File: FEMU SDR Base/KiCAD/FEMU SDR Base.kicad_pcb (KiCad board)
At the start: 4 copper layers, 164.8 x 186.6 mm, 69 parts, among them P10 PWM2, P11 PWM3, P12 PWM4, P13 PWM1, P14 PWM2, P15 PWM3, P16 PWM4, P17 12V, P18 GND, P19 12V, P2 SDR_Shield_1, P20 GND, P21 S0GND, P22 S1GND, P23 S0DN, P24 S1DN, P25 S0DP, P26 S1DP, P27 PWM0, P28 PWM5, P29 PWM6, P3 SDR_Shield_2, P30 PWM7, P31 PWM0, P32 PWM5, P33 PWM6, P34 PWM7, P4 12V, P5 GND, P6 12V, P7 GND, P8 Raspi_Power_Shield, P9 PWM1, U1 TPS562209, U2 LP38858-LDO, U3 LP38858-LDO, U4 7833, U5 7833

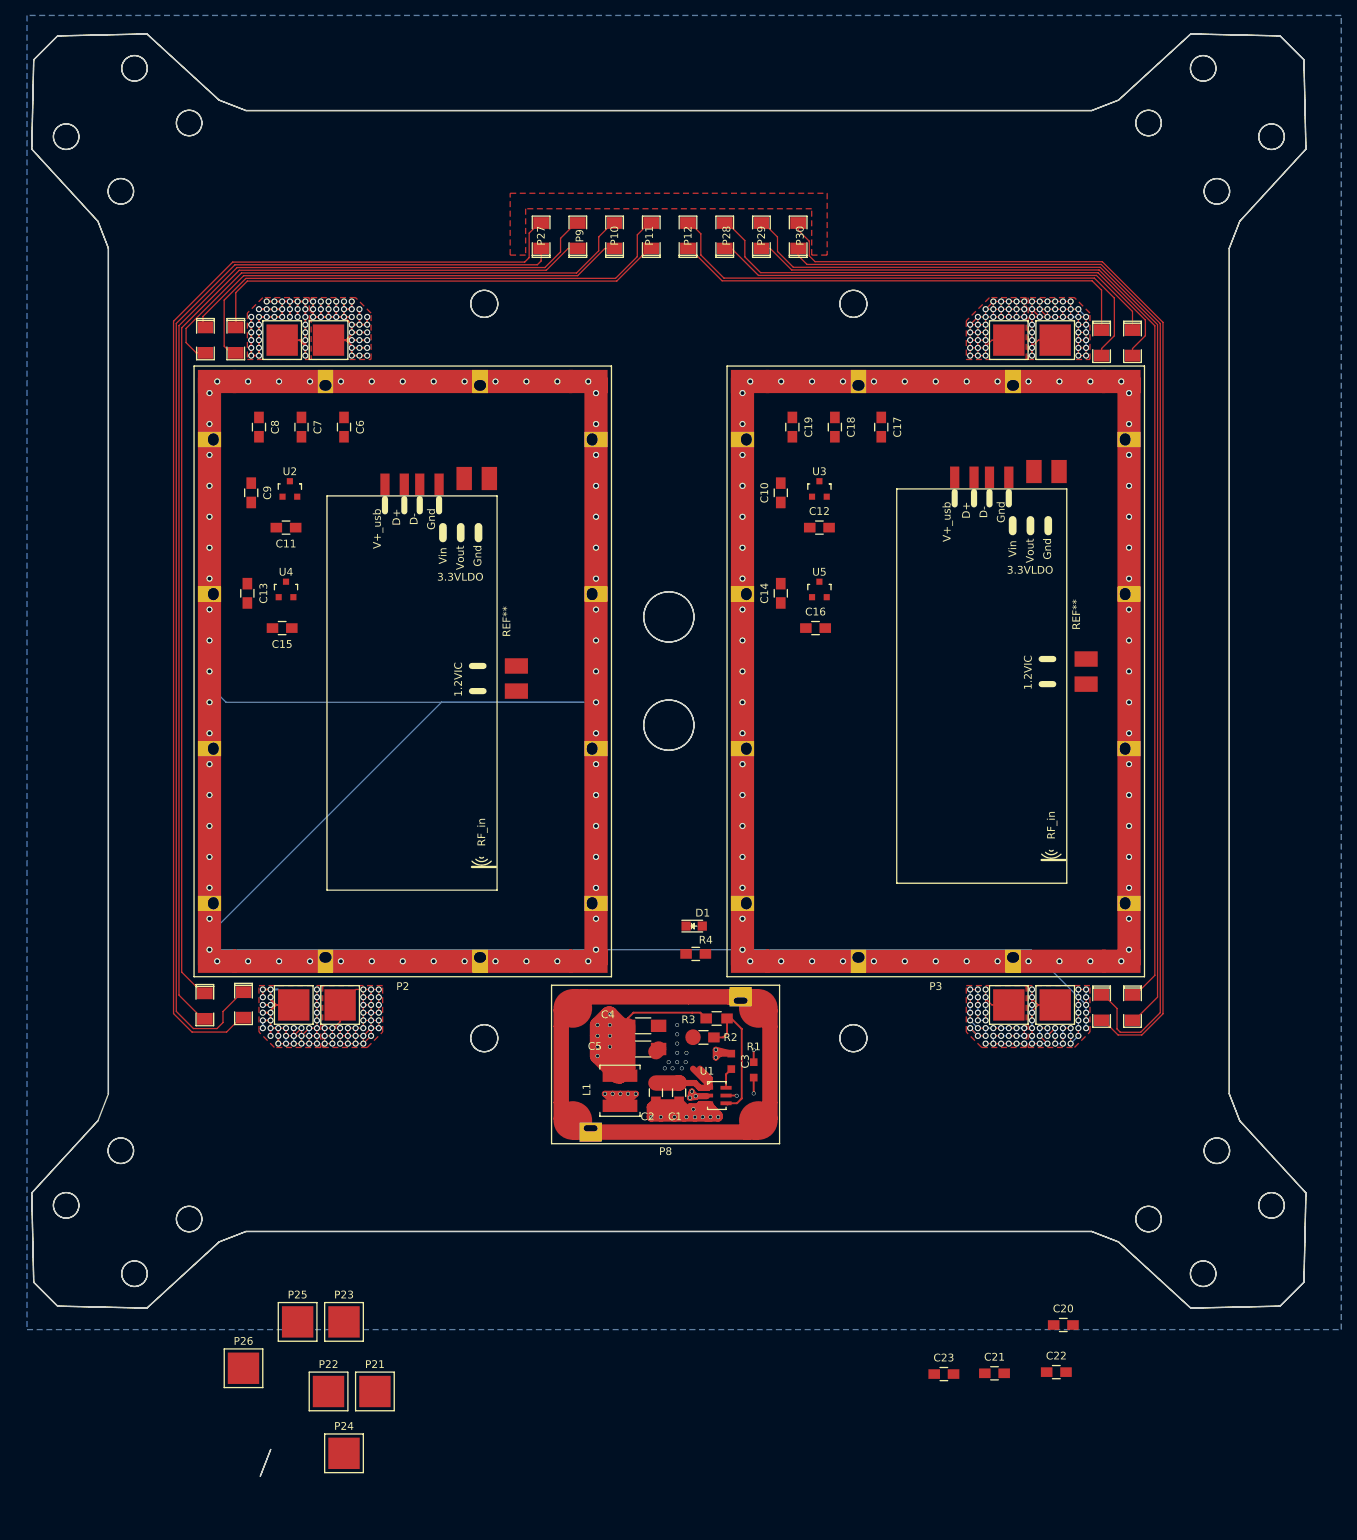
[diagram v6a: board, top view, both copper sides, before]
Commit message: Added gasket grounding
Signed-off-by: hardiepienaar <hardiepienaar@gmail.com>
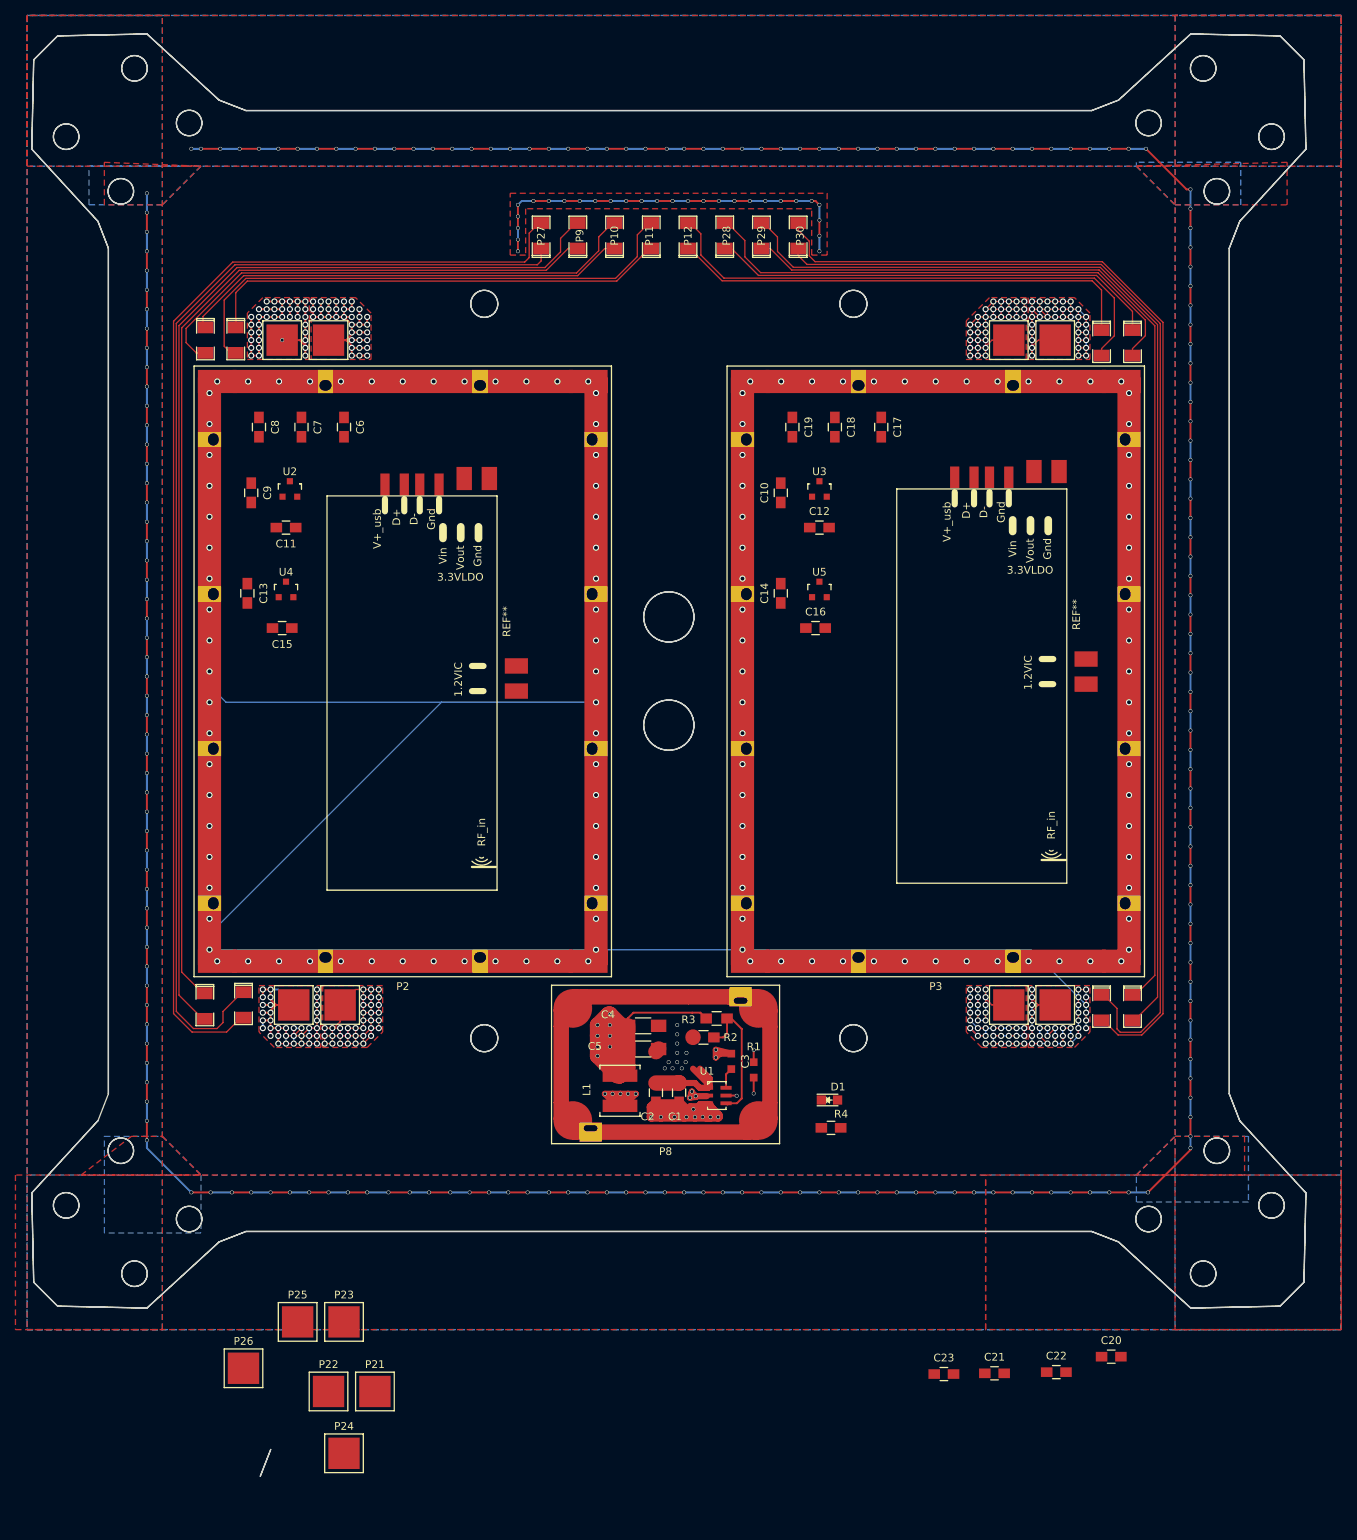
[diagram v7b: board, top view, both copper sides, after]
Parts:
- moved D1 28.5 mm to (105.3, 140.1)
- moved R4 28.5 mm to (105.5, 143.7)
- moved C20 7.43 mm to (141.8, 173.2)
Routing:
- net GND: track 911.5 -> 1542.8 mm, vias 272 -> 503
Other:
- board text added: "Do 12V and PWR ground routing Isoate signal gnd and power ground Add power plug connections Add raspi power Add pixhawk pwr Add feedthroughs Add usb isolation Add esc wire strap mounts Add SMA grounding rings Add arm grounding rings"
- board text removed: "Finish gasket grounding Do 12V and PWR ground routing Isoate signal gnd and power ground Add power plug connections Add raspi power Add pixhawk pwr Add feedthroughs Add usb isolation Add esc wire strap mounts Add SMA grounding rings Add arm grounding rings"

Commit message: Added power connections, power routing, GND isolation and cable tray grounding
Signed-off-by: hardiepienaar <hardiepienaar@gmail.com>
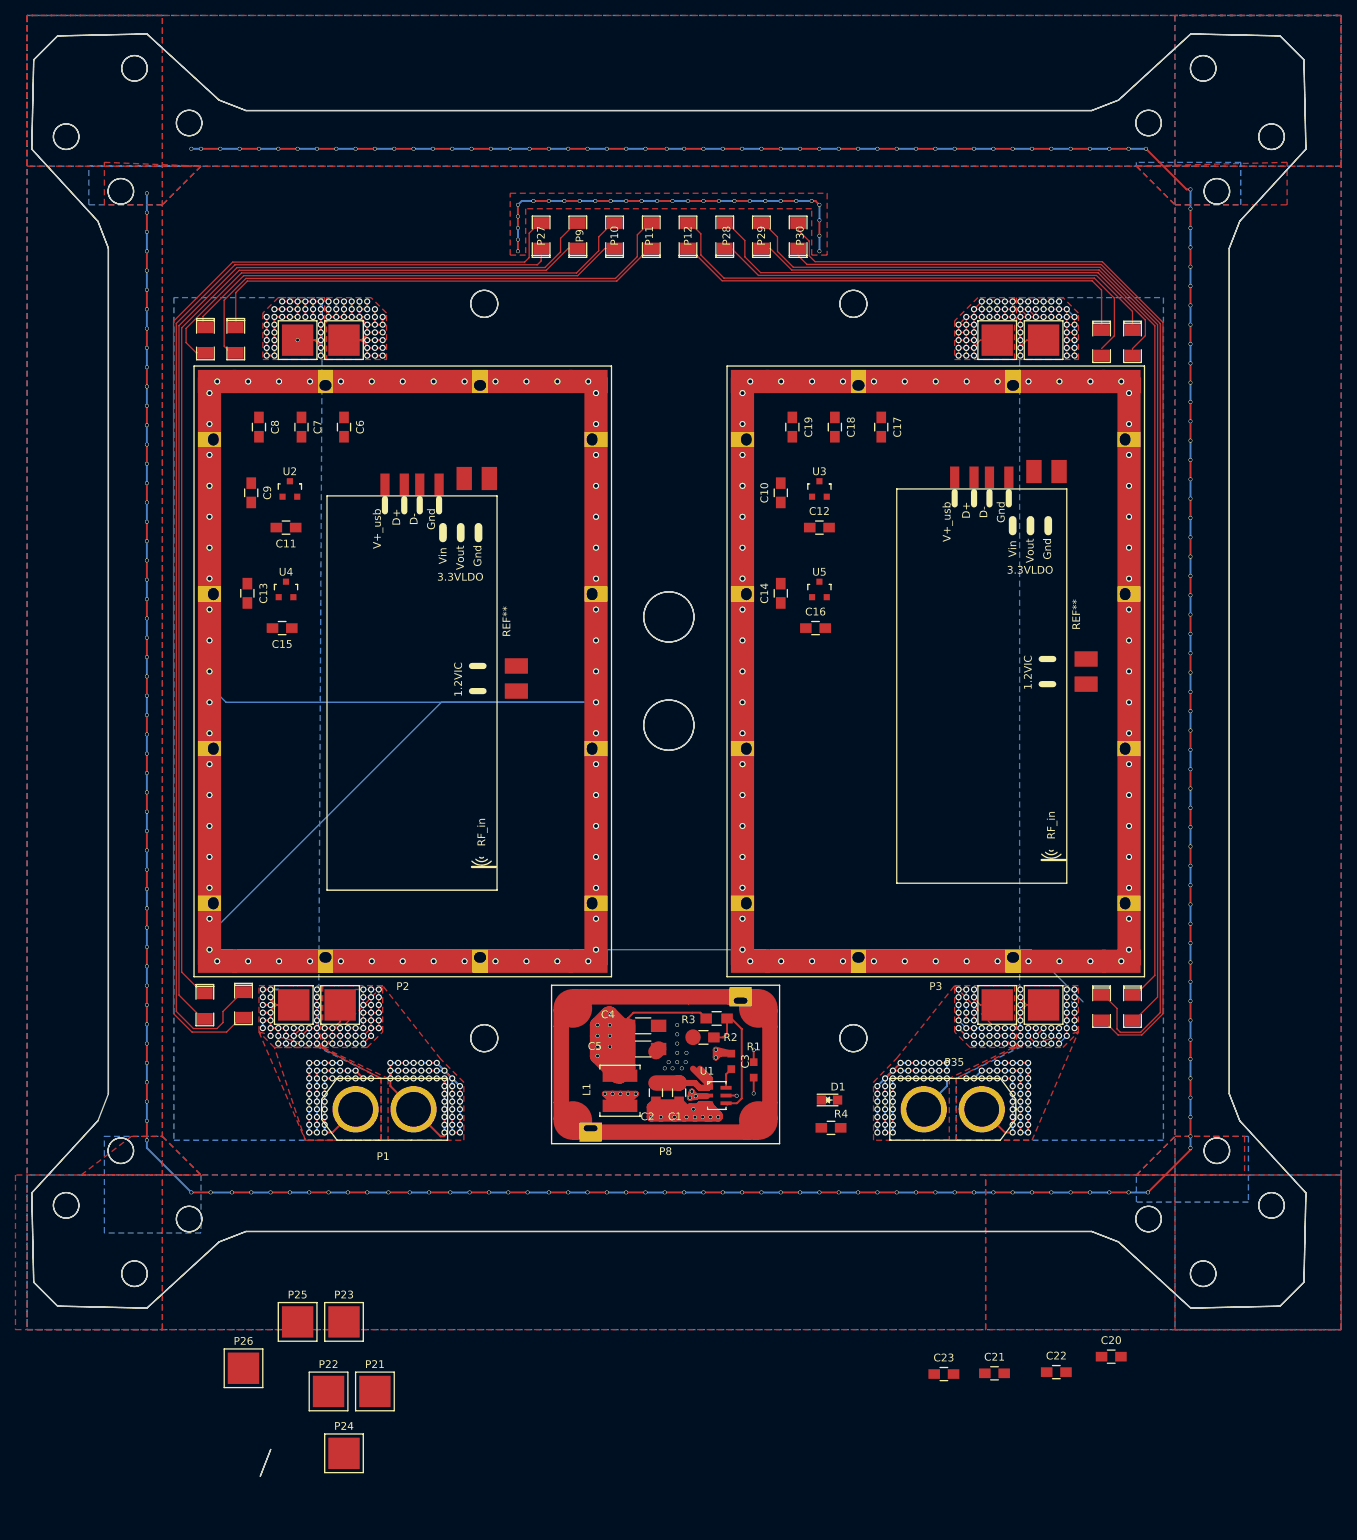
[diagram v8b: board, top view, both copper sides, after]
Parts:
- added P1: Battery, Misc footprints:XT60, F.Cu at (44.0, 141.2)
- added P35: Battery, Misc footprints:XT60, F.Cu at (125.0, 141.2)
- moved P4 2.00 mm to (42.5, 41.8)
- moved P7 2.00 mm to (36.5, 41.8)
- moved P17 1.50 mm to (127.0, 41.8)
- moved P18 1.50 mm to (133.0, 41.8)
- moved P19 1.50 mm to (127.0, 127.8)
- moved P20 1.50 mm to (133.0, 127.8)
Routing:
- net +12V: track 242.4 -> 356.6 mm, vias 151 -> 241
- net GND: track 1542.8 -> 1642.1 mm, vias 503 -> 587
- net Net-(P12-Pad2): track 68.9 -> 68.0 mm
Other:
- board text added: "Add raspi power Add pixhawk pwr Add feedthroughs Add usb isolation Add esc wire strap mounts Add SMA grounding rings Add arm grounding rings"
- board text removed: "Do 12V and PWR ground routing Isoate signal gnd and power ground Add power plug connections Add raspi power Add pixhawk pwr Add feedthroughs Add usb isolation Add esc wire strap mounts Add SMA grounding rings Add arm grounding rings"
- board text removed: "Finish cable tray copper"
- board text removed: "Power"
